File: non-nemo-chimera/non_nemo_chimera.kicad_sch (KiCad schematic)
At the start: 82 parts, among them J1 Conn_BAT, J2 Conn_BAT

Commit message: Chimera
pogopin and reset switch
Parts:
- removed J1, J2: Conn_BAT, TB2086_SMD:Molex_Pico-EZmate_78171-0002_1x02-1MP_P1.20mm_HandSolder, symbol Connector_Generic_MountingPin:Conn_01x02_MountingPin
- added J1, J2: Conn_01x02, TB2086_MISC:Tag_Pogopin_1x02_P2.54mm, symbol Connector_Generic:Conn_01x02
- added J3, J4: Conn_BAT, TB2086_SMD:Molex_Pico-EZmate_78171-0002_1x02-1MP_P1.20mm_HandSolder, symbol Connector_Generic_MountingPin:Conn_01x02_MountingPin
- added RSW1, RSW2: SMT 2X4X3.5MM Tactile Tact Push Button, TB2086_SMD:SMT 2X4X3.5MM Tactile Tact Push Button, symbol TB2086_SMD:SMT 2X4X3.5MM Tactile Tact Push Button
- renumbered D19 to D16, D20 to D17, D21 to D18, D22 to D19, D23 to D20, D24 to D21, D25 to D22, D26 to D23, D27 to D24, D28 to D25, D29 to D26, D30 to D27, D31 to D28, D32 to D29, D33 to D30, D16 to D31, D17 to D32, D18 to D33, S19 to S16, S20 to S17, S21 to S18, S22 to S19, S23 to S20, S24 to S21, S25 to S22, S26 to S23, S27 to S24, S28 to S25, S29 to S26, S30 to S27, S31 to S28, S32 to S29, S33 to S30, S16 to S31, S17 to S32, S18 to S33
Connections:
- net BAT: now also J1.1 (Pin_1)
- net BAT_r: now also J2.1 (Pin_1)
- net GND: now also J3.1 (Pin_1), J3.MP (MountPin), J4.1 (Pin_1), J4.MP (MountPin), RSW1.2, RSW2.1
- net at SW_SPDT2.2 (B): now also J4.2 (Pin_2)
- net at SW_SPDT1.2 (B): now also J3.2 (Pin_2)
- new net RST: J1.2 (Pin_2), RSW1.1
- new net RST_r: J2.2 (Pin_2), RSW2.2

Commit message: version
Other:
- title: (none) -> Non Nemo Chimera
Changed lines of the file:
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@@
 	(generator_version "8.0")
 	(paper "A3")
+	(title_block
+		(title "Non Nemo Chimera")
+		(date "2025-04-09")
+		(rev "0.2.0")
+	)
 	(junction
 		(at 357.378 201.422)

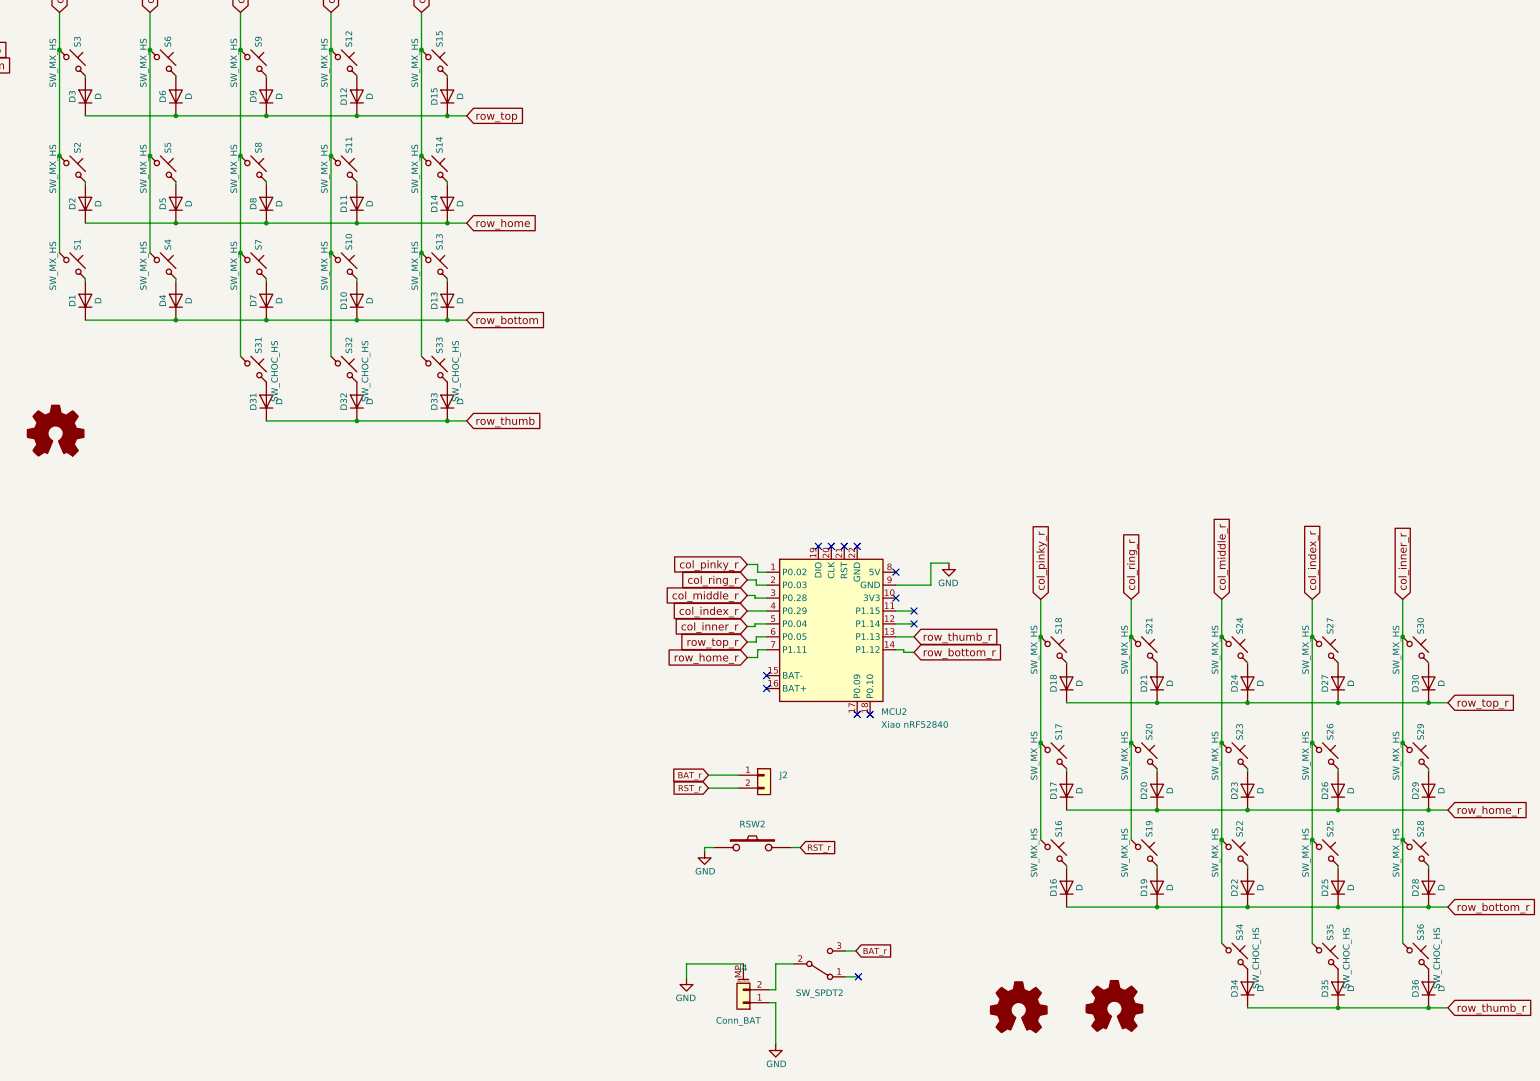
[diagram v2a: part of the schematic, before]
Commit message: fixed footprint layer for Chimera
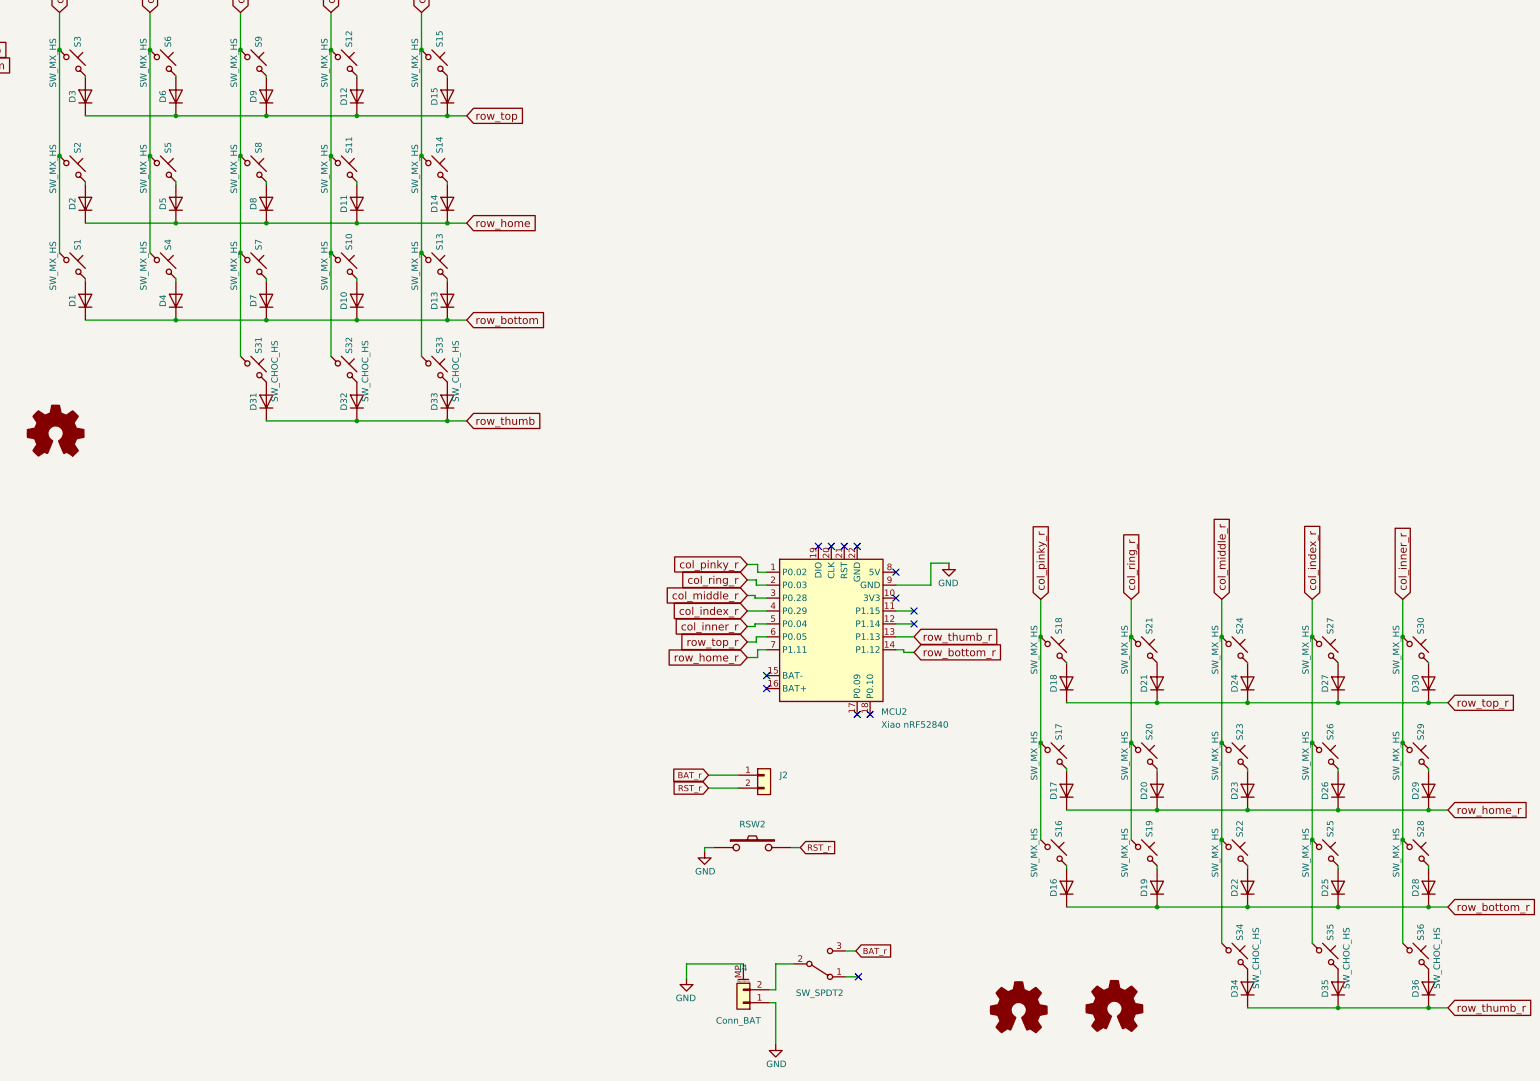
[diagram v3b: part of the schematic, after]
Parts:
- D1, D10, D11, D12, D13, D14, D15, D16, D17, D18, D19, D2, D20, D21, D22, D23, D24, D25, D26, D27, D28, D29, D3, D30, D31, D32, D33, D34, D35, D36, D4, D5, D6, D7, D8, D9: value D -> 1N4148W
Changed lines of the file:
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@@
 			)
 		)
-		(property "Value" "D"
+		(property "Value" "1N4148W"
 			(at 136.652 55.372 0)
 			(effects
@@
 					(size 1.27 1.27)
 				)
+				(hide yes)
 			)
 		)
@@
 			)
 		)
-		(property "Value" "D"
+		(property "Value" "1N4148W"
 			(at 329.438 170.688 0)
 			(effects
@@
 					(size 1.27 1.27)
 				)
+				(hide yes)
 			)
 		)
@@
 			)
 		)
-		(property "Value" "D"
+		(property "Value" "1N4148W"
 			(at 293.878 170.688 0)
 			(effects
@@
 					(size 1.27 1.27)
 				)
+				(hide yes)
 			)
 		)
@@
 			)
 		)
-		(property "Value" "D"
+		(property "Value" "1N4148W"
 			(at 118.872 76.454 0)
 			(effects
@@
 					(size 1.27 1.27)
 				)
+				(hide yes)
 			)
 		)
@@
 			)
 		)
-		(property "Value" "D"
+		(property "Value" "1N4148W"
 			(at 329.438 210.82 0)
 			(effects
@@
 					(size 1.27 1.27)
 				)
+				(hide yes)
 			)
 		)
@@
 			)
 		)
-		(property "Value" "D"
+		(property "Value" "1N4148W"
 			(at 118.872 55.372 0)
 			(effects
@@
 					(size 1.27 1.27)
 				)
+				(hide yes)
 			)
 		)
@@
 			)
 		)
-		(property "Value" "D"
+		(property "Value" "1N4148W"
 			(at 364.998 230.632 0)
 			(effects
@@
 					(size 1.27 1.27)
 				)
+				(hide yes)
 			)
 		)
@@
 			)
 		)
-		(property "Value" "D"
+		(property "Value" "1N4148W"
 			(at 118.872 95.504 0)
 			(effects
@@
 					(size 1.27 1.27)
 				)
+				(hide yes)
 			)
 		)
@@
 			)
 		)
-		(property "Value" "D"
+		(property "Value" "1N4148W"
 			(at 347.218 170.688 0)
 			(effects
@@
 					(size 1.27 1.27)
 				)
+				(hide yes)
 			)
 		)
@@
 			)
 		)
-		(property "Value" "D"
+		(property "Value" "1N4148W"
 			(at 364.998 170.688 0)
 			(effects
@@
 					(size 1.27 1.27)
 				)
+				(hide yes)
 			)
 		)
@@
 			)
 		)
-		(property "Value" "D"
+		(property "Value" "1N4148W"
 			(at 172.212 55.372 0)
 			(effects
@@
 					(size 1.27 1.27)
 				)
+				(hide yes)
 			)
 		)
@@
 			)
 		)
-		(property "Value" "D"
+		(property "Value" "1N4148W"
 			(at 154.432 95.504 0)
 			(effects
@@
 					(size 1.27 1.27)
 				)
+				(hide yes)
 			)
 		)
@@
 			)
 		)
-		(property "Value" "D"
+		(property "Value" "1N4148W"
 			(at 311.658 210.82 0)
 			(effects
@@
 					(size 1.27 1.27)
 				)
+				(hide yes)
 			)
 		)
@@
 			)
 		)
-		(property "Value" "D"
+		(property "Value" "1N4148W"
 			(at 136.652 95.504 0)
 			(effects
@@
 					(size 1.27 1.27)
 				)
+				(hide yes)
 			)
 		)
@@
 			)
 		)
-		(property "Value" "D"
+		(property "Value" "1N4148W"
 			(at 101.092 55.372 0)
 			(effects
@@
 					(size 1.27 1.27)
 				)
+				(hide yes)
 			)
 		)
@@
 			)
 		)
-		(property "Value" "D"
+		(property "Value" "1N4148W"
 			(at 172.212 115.316 0)
 			(effects
@@
 					(size 1.27 1.27)
 				)
+				(hide yes)
 			)
 		)
@@
 			)
 		)
-		(property "Value" "D"
+		(property "Value" "1N4148W"
 			(at 347.218 191.77 0)
 			(effects
@@
 					(size 1.27 1.27)
 				)
+				(hide yes)
 			)
 		)
@@
 			)
 		)
-		(property "Value" "D"
+		(property "Value" "1N4148W"
 			(at 154.432 55.372 0)
 			(effects
@@
 					(size 1.27 1.27)
 				)
+				(hide yes)
 			)
 		)
@@
 			)
 		)
-		(property "Value" "D"
+		(property "Value" "1N4148W"
 			(at 329.438 230.632 0)
 			(effects
@@
 					(size 1.27 1.27)
 				)
+				(hide yes)
 			)
 		)
@@
 			)
 		)
-		(property "Value" "D"
+		(property "Value" "1N4148W"
 			(at 364.998 191.77 0)
 			(effects
@@
 					(size 1.27 1.27)
 				)
+				(hide yes)
 			)
 		)
@@
 			)
 		)
-		(property "Value" "D"
+		(property "Value" "1N4148W"
 			(at 154.432 76.454 0)
 			(effects
@@
 					(size 1.27 1.27)
 				)
+				(hide yes)
 			)
 		)
@@
 			)
 		)
-		(property "Value" "D"
+		(property "Value" "1N4148W"
 			(at 154.432 115.316 0)
 			(effects
@@
 					(size 1.27 1.27)
 				)
+				(hide yes)
 			)
 		)
@@
 			)
 		)
-		(property "Value" "D"
+		(property "Value" "1N4148W"
 			(at 136.652 76.454 0)
 			(effects
@@
 					(size 1.27 1.27)
 				)
+				(hide yes)
 			)
 		)
@@
 			)
 		)
-		(property "Value" "D"
+		(property "Value" "1N4148W"
 			(at 172.212 76.454 0)
 			(effects
@@
 					(size 1.27 1.27)
 				)
+				(hide yes)
 			)
 		)
@@
 			)
 		)
-		(property "Value" "D"
+		(property "Value" "1N4148W"
 			(at 364.998 210.82 0)
 			(effects
@@
 					(size 1.27 1.27)
 				)
+				(hide yes)
 			)
 		)
@@
 			)
 		)
-		(property "Value" "D"
+		(property "Value" "1N4148W"
 			(at 172.212 95.504 0)
 			(effects
@@
 					(size 1.27 1.27)
 				)
+				(hide yes)
 			)
 		)
@@
 			)
 		)
-		(property "Value" "D"
+		(property "Value" "1N4148W"
 			(at 101.092 76.454 0)
 			(effects
@@
 					(size 1.27 1.27)
 				)
+				(hide yes)
 			)
 		)
@@
 			)
 		)
-		(property "Value" "D"
+		(property "Value" "1N4148W"
 			(at 293.878 210.82 0)
 			(effects
@@
 					(size 1.27 1.27)
 				)
+				(hide yes)
 			)
 		)
@@
 			)
 		)
-		(property "Value" "D"
+		(property "Value" "1N4148W"
 			(at 347.218 210.82 0)
 			(effects
@@
 					(size 1.27 1.27)
 				)
+				(hide yes)
 			)
 		)
@@
 			)
 		)
-		(property "Value" "D"
+		(property "Value" "1N4148W"
 			(at 136.652 115.316 0)
 			(effects
@@
 					(size 1.27 1.27)
 				)
+				(hide yes)
 			)
 		)
@@
 			)
 		)
-		(property "Value" "D"
+		(property "Value" "1N4148W"
 			(at 329.438 191.77 0)
 			(effects
@@
 					(size 1.27 1.27)
 				)
+				(hide yes)
 			)
 		)
@@
 			)
 		)
-		(property "Value" "D"
+		(property "Value" "1N4148W"
 			(at 347.218 230.632 0)
 			(effects
@@
 					(size 1.27 1.27)
 				)
+				(hide yes)
 			)
 		)
@@
 			)
 		)
-		(property "Value" "D"
+		(property "Value" "1N4148W"
 			(at 311.658 170.688 0)
 			(effects
@@
 					(size 1.27 1.27)
 				)
+				(hide yes)
 			)
 		)
@@
 			)
 		)
-		(property "Value" "D"
+		(property "Value" "1N4148W"
 			(at 293.878 191.77 0)
 			(effects
@@
 					(size 1.27 1.27)
 				)
+				(hide yes)
 			)
 		)
@@
 			)
 		)
-		(property "Value" "D"
+		(property "Value" "1N4148W"
 			(at 311.658 191.77 0)
 			(effects
@@
 					(size 1.27 1.27)
 				)
+				(hide yes)
 			)
 		)
@@
 			)
 		)
-		(property "Value" "D"
+		(property "Value" "1N4148W"
 			(at 101.092 95.504 0)
 			(effects
@@
 					(size 1.27 1.27)
 				)
+				(hide yes)
 			)
 		)
